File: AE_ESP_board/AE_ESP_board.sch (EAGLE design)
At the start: 28 parts, among them CN1 SW_UART_IF, CN2 HW_UART_IF, CN3 POWER_IF, Q1 2N7000, Q2 2N7000, SW1 10-XX, U1 AE-ESP-WROOM-02, U4 XC6202P332TH

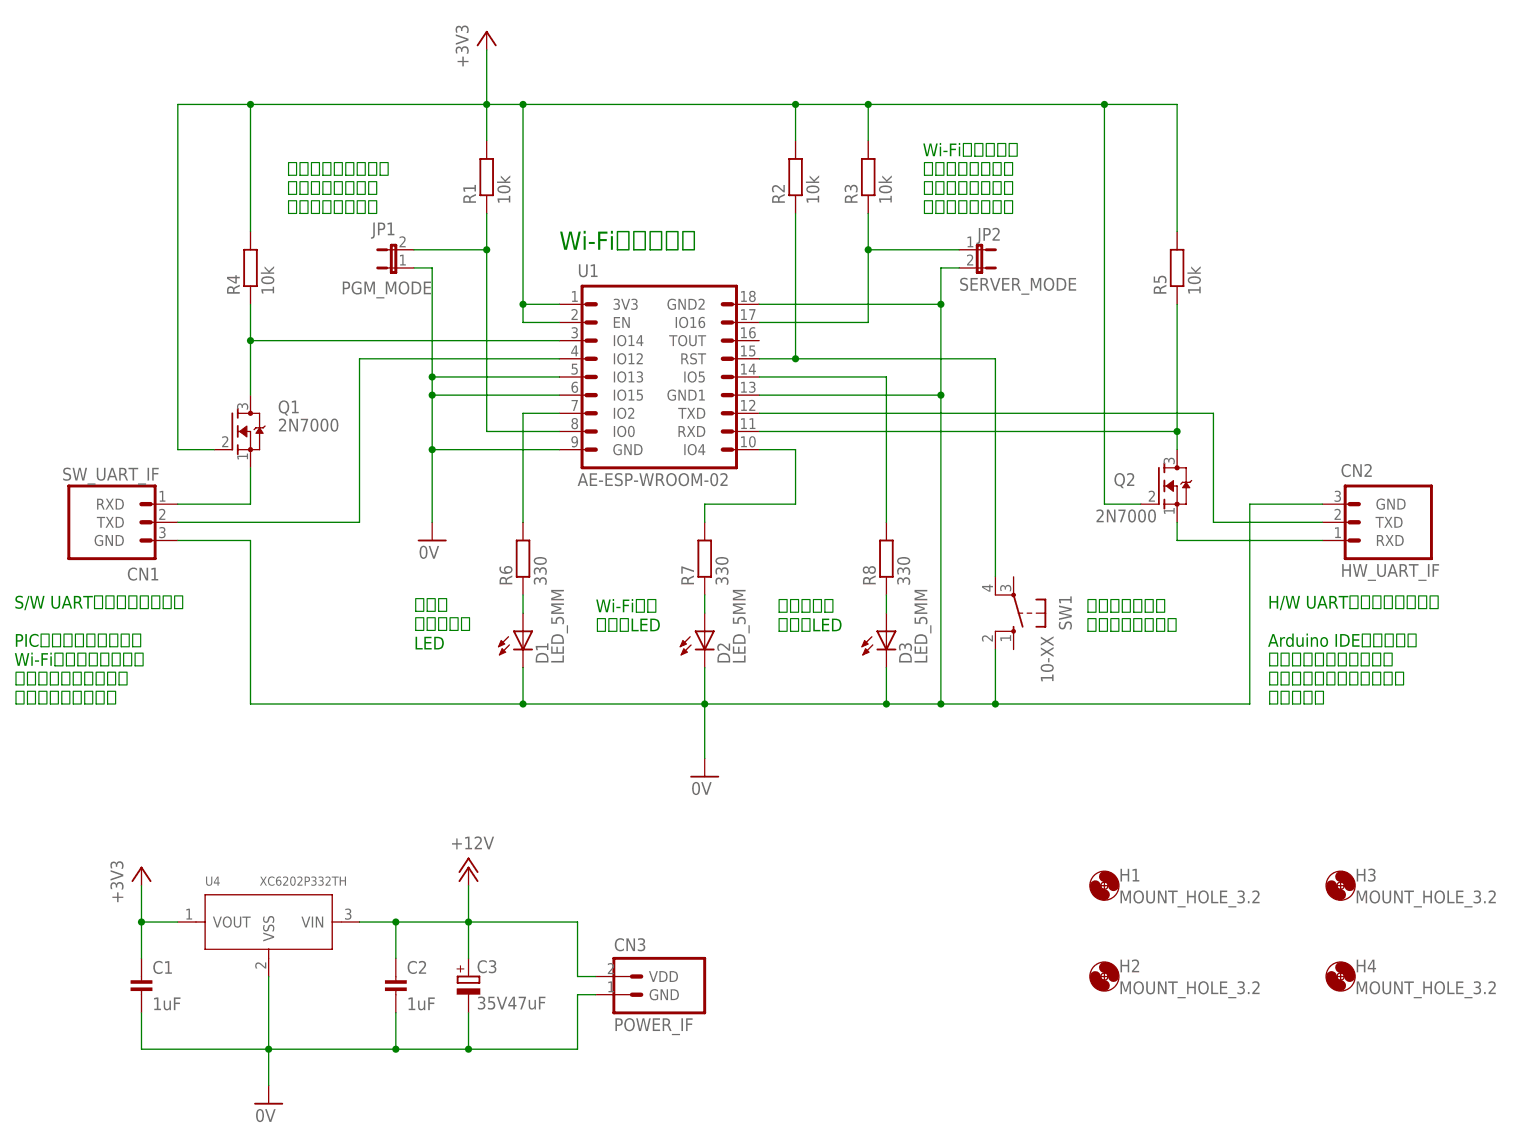
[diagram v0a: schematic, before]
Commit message: 回路図を修正
150mA —> 500mAのCMOSレギュレーターに変更
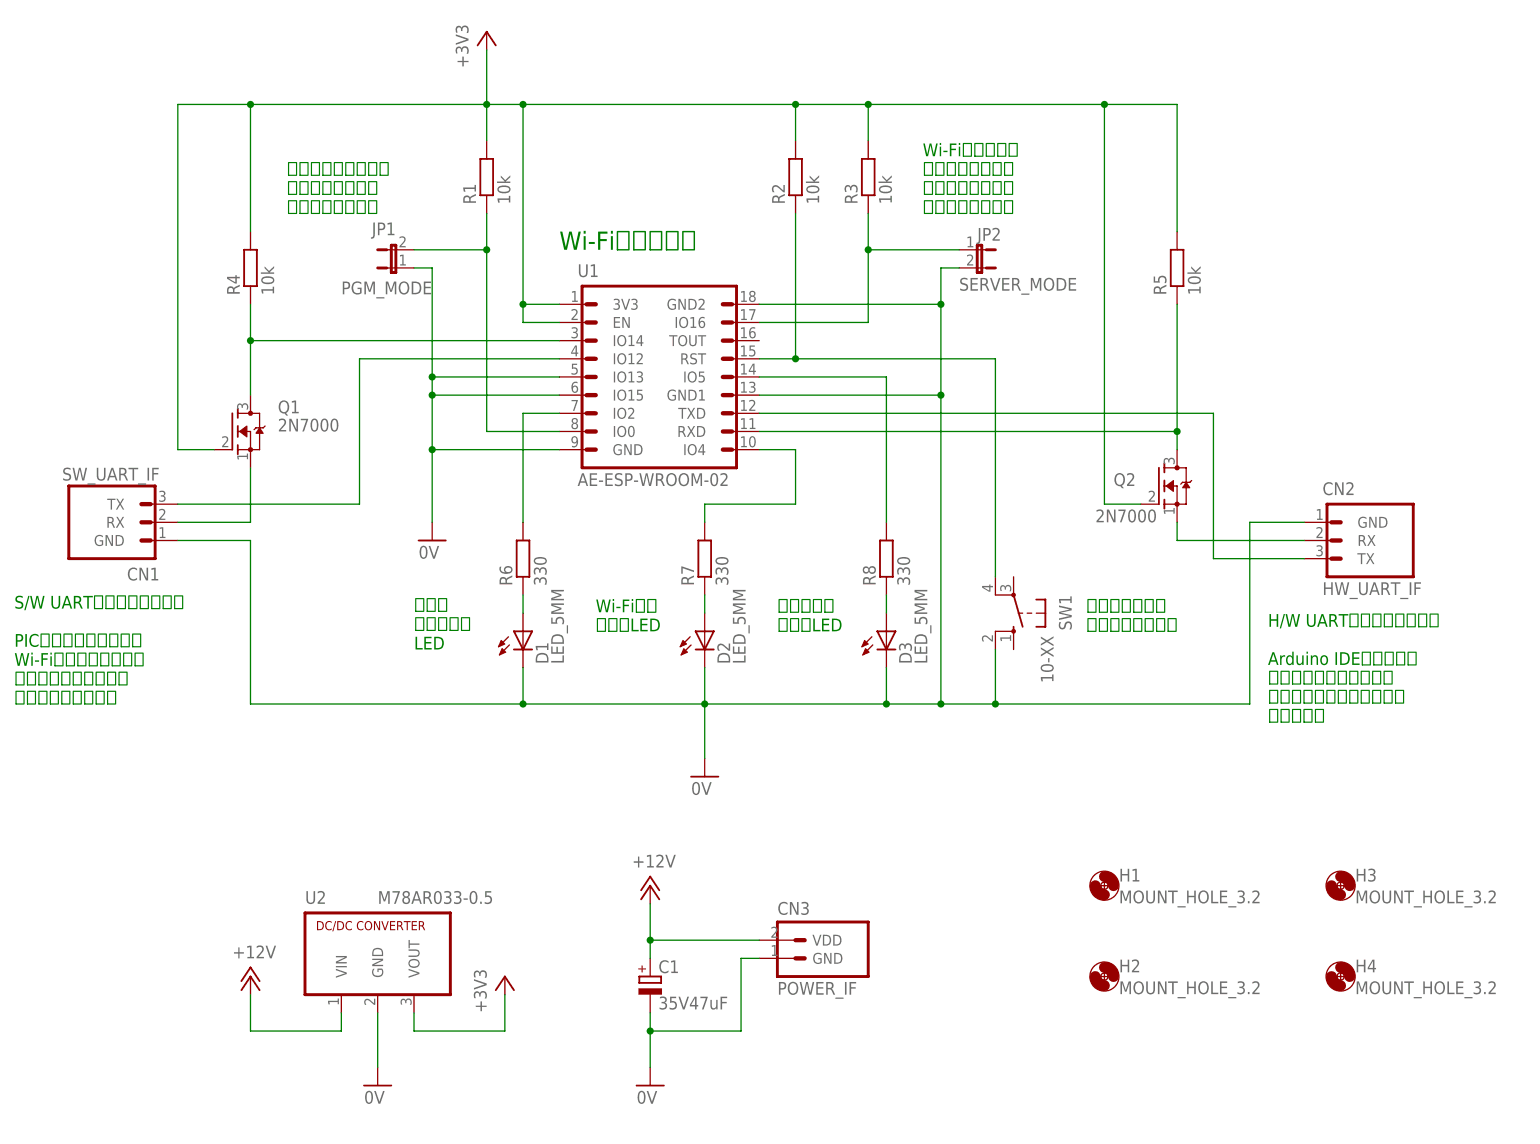
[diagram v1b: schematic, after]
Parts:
- removed C2: 1uF, Parts:CAP_200MIL
- removed C3: 35V47uF, Parts:ELECAP_200MIL
- removed U4: XC6202P332TH, Parts:XC6202P332TH
- added U2: M78AR033-0.5, Parts:M78AR033-0.5
- C1: value 1uF -> 35V47uF; device Parts:CAP_200MIL -> Parts:ELECAP_200MIL
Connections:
- removed net HW_UART_RXD: CN2.RXD, Q2.S
- new net N$3: CN2.RX, Q2.S
- net +12V: now also C1.+, U2.VIN; no longer C2.1, C3.+, U4.VIN
- net +3V3: now also U2.VOUT; no longer C1.1, U4.VOUT
- net 0V: now also C1.-, U2.GND; no longer C1.2, C2.2, C3.-, U4.VSS
- net HW_UART_TXD: now also CN2.TX; no longer CN2.TXD
- net N$1: now also CN1.TX; no longer CN1.TXD
- net SW_UART_RXD: now also CN1.RX; no longer CN1.RXD
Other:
- moved on the sheet: CN2, CN3

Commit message: 回路図を修正
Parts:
- C1: device Parts:ELECAP_200MIL -> Parts:ELECAP_D5_100MIL
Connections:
- net 0V: now also SW1.S
- net N$10: now also SW1.P
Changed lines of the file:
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@@
 <part name="Q1" library="Parts" deviceset="2N7000" device=""/>
 <part name="R4" library="Parts" deviceset="RESISTOR" device="_200MIL" value="10k"/>
-<part name="C1" library="Parts" deviceset="ELECAP" device="_200MIL" value="35V47uF"/>
+<part name="C1" library="Parts" deviceset="ELECAP" device="_D5_100MIL" value="35V47uF"/>
 <part name="P+1" library="Supply" deviceset="+12V" device=""/>
 <part name="H1" library="Generic" deviceset="MOUNT_HOLE" device="_3.2"/>
@@
 <junction x="124.46" y="71.12"/>
 <pinref part="SW1" gate="1" pin="S1"/>
-<wire x1="165.1" y1="78.74" x2="165.1" y2="71.12" width="0.1524" layer="91"/>
+<wire x1="165.1" y1="78.74" x2="165.1" y2="76.2" width="0.1524" layer="91"/>
+<wire x1="165.1" y1="76.2" x2="165.1" y2="71.12" width="0.1524" layer="91"/>
 <wire x1="165.1" y1="71.12" x2="157.48" y2="71.12" width="0.1524" layer="91"/>
 <wire x1="157.48" y1="71.12" x2="149.86" y2="71.12" width="0.1524" layer="91"/>
@@
 <pinref part="CN1" gate="G$1" pin="GND"/>
 <wire x1="50.8" y1="93.98" x2="60.96" y2="93.98" width="0.1524" layer="91"/>
+<pinref part="SW1" gate="1" pin="S"/>
+<wire x1="167.64" y1="78.74" x2="167.64" y2="76.2" width="0.1524" layer="91"/>
+<wire x1="167.64" y1="76.2" x2="165.1" y2="76.2" width="0.1524" layer="91"/>
+<junction x="165.1" y="76.2"/>
 </segment>
 <segment>
@@
 <pinref part="SW1" gate="1" pin="P1"/>
 <wire x1="137.16" y1="119.38" x2="132.08" y2="119.38" width="0.1524" layer="91"/>
-<wire x1="165.1" y1="119.38" x2="165.1" y2="88.9" width="0.1524" layer="91"/>
+<wire x1="165.1" y1="119.38" x2="165.1" y2="91.44" width="0.1524" layer="91"/>
 <pinref part="R2" gate="G$1" pin="1"/>
+<wire x1="165.1" y1="91.44" x2="165.1" y2="88.9" width="0.1524" layer="91"/>
 <wire x1="137.16" y1="139.7" x2="137.16" y2="119.38" width="0.1524" layer="91"/>
 <junction x="137.16" y="119.38"/>
-</segment>
-</net>
+<pinref part="SW1" gate="1" pin="P"/>
+<wire x1="167.64" y1="88.9" x2="167.64" y2="91.44" width="0.1524" layer="91"/>
+<wire x1="167.64" y1="91.44" x2="165.1" y2="91.44" width="0.1524" layer="91"/>
+<junction x="165.1" y="91.44"/>
+</segment>
+</net>

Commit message: レイアウトを大幅見直し
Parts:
- D1, D2, D3: value LED_5MM -> LED_0805; device Parts:LED_5MM -> Parts:LED_0805
- R6, R7, R8: device Parts:RESISTOR_200MIL -> Parts:RESISTOR_0805
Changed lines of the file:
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@@
 <part name="R2" library="Parts" deviceset="RESISTOR" device="_200MIL" value="10k"/>
 <part name="R1" library="Parts" deviceset="RESISTOR" device="_200MIL" value="10k"/>
-<part name="D1" library="Parts" deviceset="LED" device="_5MM"/>
-<part name="D2" library="Parts" deviceset="LED" device="_5MM"/>
-<part name="R6" library="Parts" deviceset="RESISTOR" device="_200MIL" value="330"/>
-<part name="R7" library="Parts" deviceset="RESISTOR" device="_200MIL" value="330"/>
+<part name="D1" library="Parts" deviceset="LED" device="_0805" value="LED_0805"/>
+<part name="D2" library="Parts" deviceset="LED" device="_0805" value="LED_0805"/>
+<part name="R6" library="Parts" deviceset="RESISTOR" device="_0805" value="330"/>
+<part name="R7" library="Parts" deviceset="RESISTOR" device="_0805" value="330"/>
 <part name="GND12" library="Supply" deviceset="0V" device=""/>
 <part name="JP1" library="Parts" deviceset="JP1E" device="" value="PGM_MODE"/>
@@
 <part name="JP2" library="Parts" deviceset="JP1E" device="" value="SERVER_MODE"/>
 <part name="R3" library="Parts" deviceset="RESISTOR" device="_200MIL" value="10k"/>
-<part name="R8" library="Parts" deviceset="RESISTOR" device="_200MIL" value="330"/>
-<part name="D3" library="Parts" deviceset="LED" device="_5MM"/>
+<part name="R8" library="Parts" deviceset="RESISTOR" device="_0805" value="330"/>
+<part name="D3" library="Parts" deviceset="LED" device="_0805" value="LED_0805"/>
 <part name="CN2" library="PartsForProto" deviceset="UART_IF" device="" value="HW_UART_IF"/>
 <part name="CN1" library="PartsForProto" deviceset="UART_IF" device="" value="SW_UART_IF"/>

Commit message: レイアウト見直し
LED以外はリード部品とする
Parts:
- R6, R7, R8: device Parts:RESISTOR_0805 -> Parts:RESISTOR_200MIL
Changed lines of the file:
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@@
 <part name="D1" library="Parts" deviceset="LED" device="_0805" value="LED_0805"/>
 <part name="D2" library="Parts" deviceset="LED" device="_0805" value="LED_0805"/>
-<part name="R6" library="Parts" deviceset="RESISTOR" device="_0805" value="330"/>
-<part name="R7" library="Parts" deviceset="RESISTOR" device="_0805" value="330"/>
+<part name="R6" library="Parts" deviceset="RESISTOR" device="_200MIL" value="330"/>
+<part name="R7" library="Parts" deviceset="RESISTOR" device="_200MIL" value="330"/>
 <part name="GND12" library="Supply" deviceset="0V" device=""/>
 <part name="JP1" library="Parts" deviceset="JP1E" device="" value="PGM_MODE"/>
@@
 <part name="JP2" library="Parts" deviceset="JP1E" device="" value="SERVER_MODE"/>
 <part name="R3" library="Parts" deviceset="RESISTOR" device="_200MIL" value="10k"/>
-<part name="R8" library="Parts" deviceset="RESISTOR" device="_0805" value="330"/>
+<part name="R8" library="Parts" deviceset="RESISTOR" device="_200MIL" value="330"/>
 <part name="D3" library="Parts" deviceset="LED" device="_0805" value="LED_0805"/>
 <part name="CN2" library="PartsForProto" deviceset="UART_IF" device="" value="HW_UART_IF"/>

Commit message: LEDを表面実装にする理由がないので、こちらもリード部品化 （ただし3mm砲弾型前提）
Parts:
- D1, D2, D3: value LED_0805 -> LED_3MM; device Parts:LED_0805 -> Parts:LED_3MM
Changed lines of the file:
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@@
 <part name="R2" library="Parts" deviceset="RESISTOR" device="_200MIL" value="10k"/>
 <part name="R1" library="Parts" deviceset="RESISTOR" device="_200MIL" value="10k"/>
-<part name="D1" library="Parts" deviceset="LED" device="_0805" value="LED_0805"/>
-<part name="D2" library="Parts" deviceset="LED" device="_0805" value="LED_0805"/>
+<part name="D1" library="Parts" deviceset="LED" device="_3MM" value="LED_3MM"/>
+<part name="D2" library="Parts" deviceset="LED" device="_3MM" value="LED_3MM"/>
 <part name="R6" library="Parts" deviceset="RESISTOR" device="_200MIL" value="330"/>
 <part name="R7" library="Parts" deviceset="RESISTOR" device="_200MIL" value="330"/>
@@
 <part name="R3" library="Parts" deviceset="RESISTOR" device="_200MIL" value="10k"/>
 <part name="R8" library="Parts" deviceset="RESISTOR" device="_200MIL" value="330"/>
-<part name="D3" library="Parts" deviceset="LED" device="_0805" value="LED_0805"/>
+<part name="D3" library="Parts" deviceset="LED" device="_3MM" value="LED_3MM"/>
 <part name="CN2" library="PartsForProto" deviceset="UART_IF" device="" value="HW_UART_IF"/>
 <part name="CN1" library="PartsForProto" deviceset="UART_IF" device="" value="SW_UART_IF"/>
